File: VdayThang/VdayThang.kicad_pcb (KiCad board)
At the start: 2 copper layers, 101.6 x 101.6 mm, 0 parts

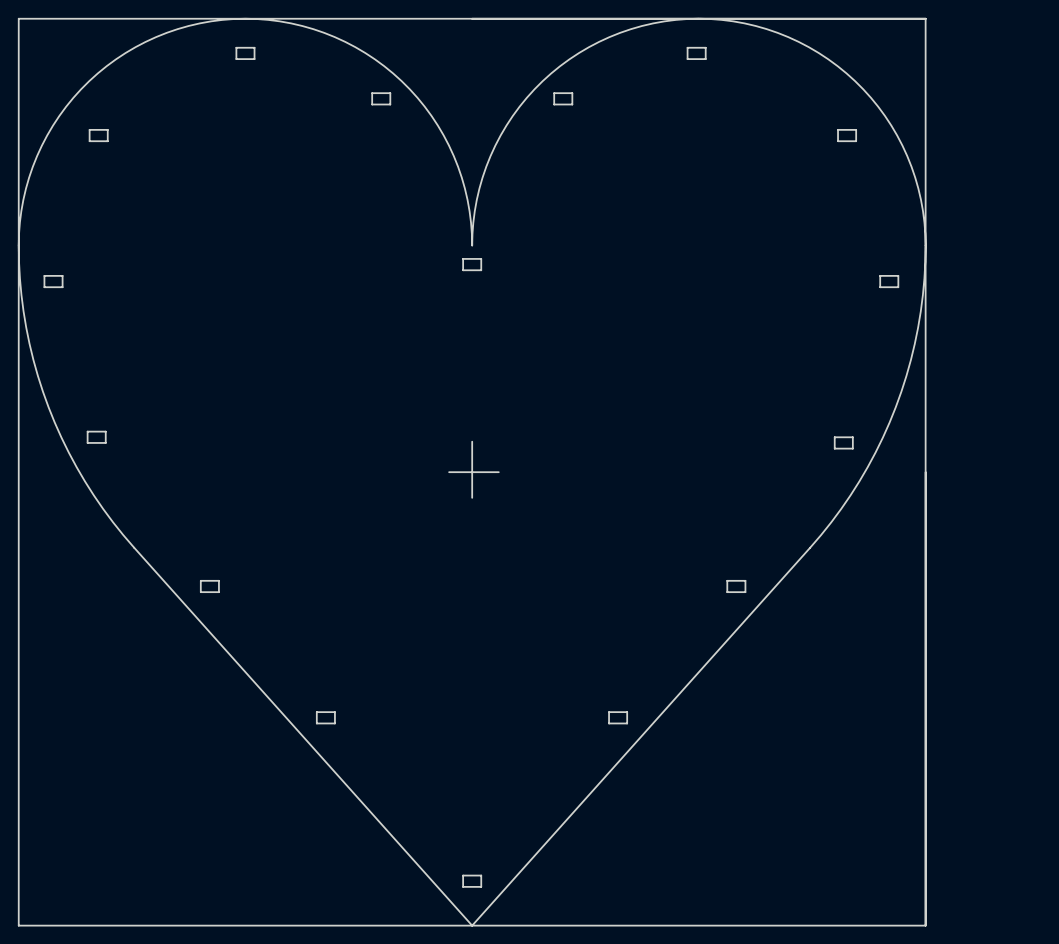
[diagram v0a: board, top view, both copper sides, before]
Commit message: placed footprints
finished basic footprint layout
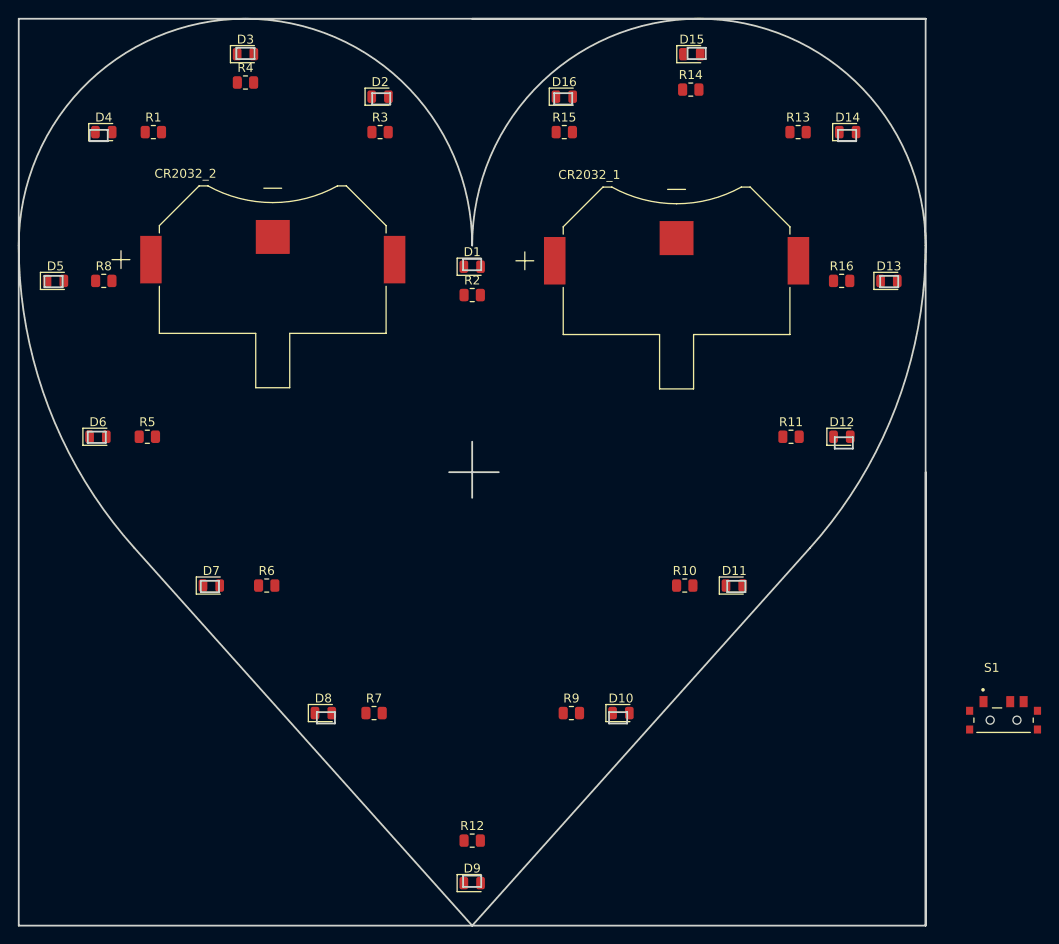
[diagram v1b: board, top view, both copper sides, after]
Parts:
- added CR2032_1: Battery, LogansCustom:BAT_CR2032, F.Cu at (166.6, 70.8)
- added CR2032_2: Battery, LogansCustom:BAT_CR2032, F.Cu at (121.3, 70.6)
- added D1: LED, LED_SMD:LED_0805_2012Metric, F.Cu at (143.7, 71.4)
- added D10: LED, LED_SMD:LED_0805_2012Metric, F.Cu at (160.3, 121.4)
- added D11: LED, LED_SMD:LED_0805_2012Metric, F.Cu at (173.0, 107.2)
- added D12: LED, LED_SMD:LED_0805_2012Metric, F.Cu at (185.1, 90.5)
- added D13: LED, LED_SMD:LED_0805_2012Metric, F.Cu at (190.4, 73.0)
- added D14: LED, LED_SMD:LED_0805_2012Metric, F.Cu at (185.7, 56.4)
- added D15: LED, LED_SMD:LED_0805_2012Metric, F.Cu at (168.3, 47.6)
- added D16: LED, LED_SMD:LED_0805_2012Metric, F.Cu at (154.0, 52.4)
- added D2: LED, LED_SMD:LED_0805_2012Metric, F.Cu at (133.3, 52.4)
- added D3: LED, LED_SMD:LED_0805_2012Metric, F.Cu at (118.3, 47.6)
- added D4: LED, LED_SMD:LED_0805_2012Metric, F.Cu at (102.4, 56.4)
- added D5: LED, LED_SMD:LED_0805_2012Metric, F.Cu at (97.0, 73.0)
- added D6: LED, LED_SMD:LED_0805_2012Metric, F.Cu at (101.7, 90.5)
- added D7: LED, LED_SMD:LED_0805_2012Metric, F.Cu at (114.4, 107.2)
- added D8: LED, LED_SMD:LED_0805_2012Metric, F.Cu at (127.0, 121.4)
- added D9: LED, LED_SMD:LED_0805_2012Metric, F.Cu at (143.7, 140.5)
- added R1: R, Resistor_SMD:R_0805_2012Metric, F.Cu at (108.0, 56.4)
- added R10: R, Resistor_SMD:R_0805_2012Metric, F.Cu at (167.5, 107.2)
- added R11: R, Resistor_SMD:R_0805_2012Metric, F.Cu at (179.4, 90.5)
- added R12: R, Resistor_SMD:R_0805_2012Metric, F.Cu at (143.7, 135.7)
- added R13: R, Resistor_SMD:R_0805_2012Metric, F.Cu at (180.2, 56.4)
- added R14: R, Resistor_SMD:R_0805_2012Metric, F.Cu at (168.2, 51.6)
- added R15: R, Resistor_SMD:R_0805_2012Metric, F.Cu at (154.0, 56.4)
- added R16: R, Resistor_SMD:R_0805_2012Metric, F.Cu at (185.1, 73.0)
- added R2: R, Resistor_SMD:R_0805_2012Metric, F.Cu at (143.7, 74.6)
- added R3: R, Resistor_SMD:R_0805_2012Metric, F.Cu at (133.3, 56.4)
- added R4: R, Resistor_SMD:R_0805_2012Metric, F.Cu at (118.3, 50.8)
- added R5: R, Resistor_SMD:R_0805_2012Metric, F.Cu at (107.3, 90.5)
- added R6: R, Resistor_SMD:R_0805_2012Metric, F.Cu at (120.7, 107.2)
- added R7: R, Resistor_SMD:R_0805_2012Metric, F.Cu at (132.7, 121.4)
- added R8: R, Resistor_SMD:R_0805_2012Metric, F.Cu at (102.4, 73.0)
- added R9: R, Resistor_SMD:R_0805_2012Metric, F.Cu at (154.8, 121.4)
- added S1: SLW-66527511-SMT-TR, LogansCustom:SW_SLW-66527511-SMT-TR, F.Cu at (203.2, 122.2)

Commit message: Routing and Footprints done
Finished routing board, made cr2032 holder footprint. Still need to add edge cuts.
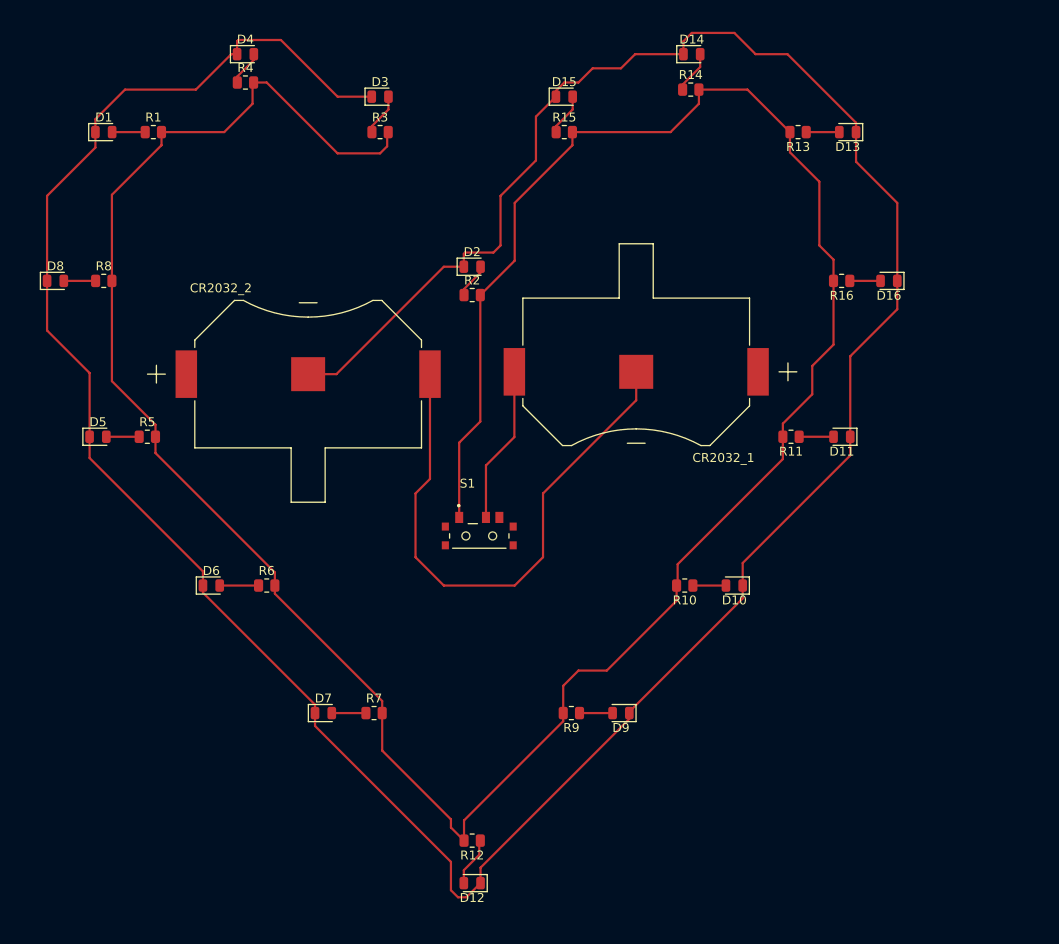
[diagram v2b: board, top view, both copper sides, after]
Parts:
- S1: value SLW-66527511-SMT-TR -> ~
- moved S1 62.3 mm to (144.5, 101.6)
- moved CR2032_2 13.4 mm to (125.3, 83.5)
- moved CR2032_1 13.2 mm to (162.0, 83.2), turned to 180 degrees
- turned D10 to 180 degrees
- turned D11 to 180 degrees
- turned D12 to 180 degrees
- turned D13 to 180 degrees
- turned D16 to 180 degrees
- turned D9 to 180 degrees
- turned R10 to 180 degrees
- turned R11 to 180 degrees
- turned R12 to 180 degrees
- turned R13 to 180 degrees
- turned R16 to 180 degrees
- turned R9 to 180 degrees
- renumbered D4 to D1, D11 to D10, D12 to D11, D9 to D12, D14 to D13, D15 to D14, D16 to D15, D13 to D16, D1 to D2, D2 to D3, D3 to D4, D6 to D5, D7 to D6, D8 to D7, D5 to D8, D10 to D9
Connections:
- S1 pad 1: unconnected-(S1-Pad1) -> 3v
- S1 pad 3: 3v -> unconnected-(S1-Pad3)
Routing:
- net -: track 0.00 -> 345.8 mm
- net 3v: track 0.00 -> 310.2 mm
- net Net-(CR2032_1--): track 0.00 -> 63.2 mm
- net Net-(CR2032_1-+): track 0.00 -> 17.6 mm
- net Net-(D12-A): track 0.00 -> 5.53 mm
- net Net-(D14-A): track 0.00 -> 4.78 mm
- net Net-(D15-A): track 0.00 -> 4.74 mm
- net Net-(D3-A): track 0.00 -> 4.74 mm
- net Net-(D6-A): track 0.00 -> 4.36 mm
- net Net-(D2-A): track 0.00 -> 4.19 mm
- net Net-(D4-A): track 0.00 -> 3.94 mm
- net Net-(D11-A): track 0.00 -> 3.85 mm
- net Net-(D7-A): track 0.00 -> 3.82 mm
- net Net-(D9-A): track 0.00 -> 3.71 mm
- net Net-(D13-A): track 0.00 -> 3.71 mm
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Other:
- board outline removed

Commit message: Finished :0
layout done, BOM done, just need to print, etch, assemble
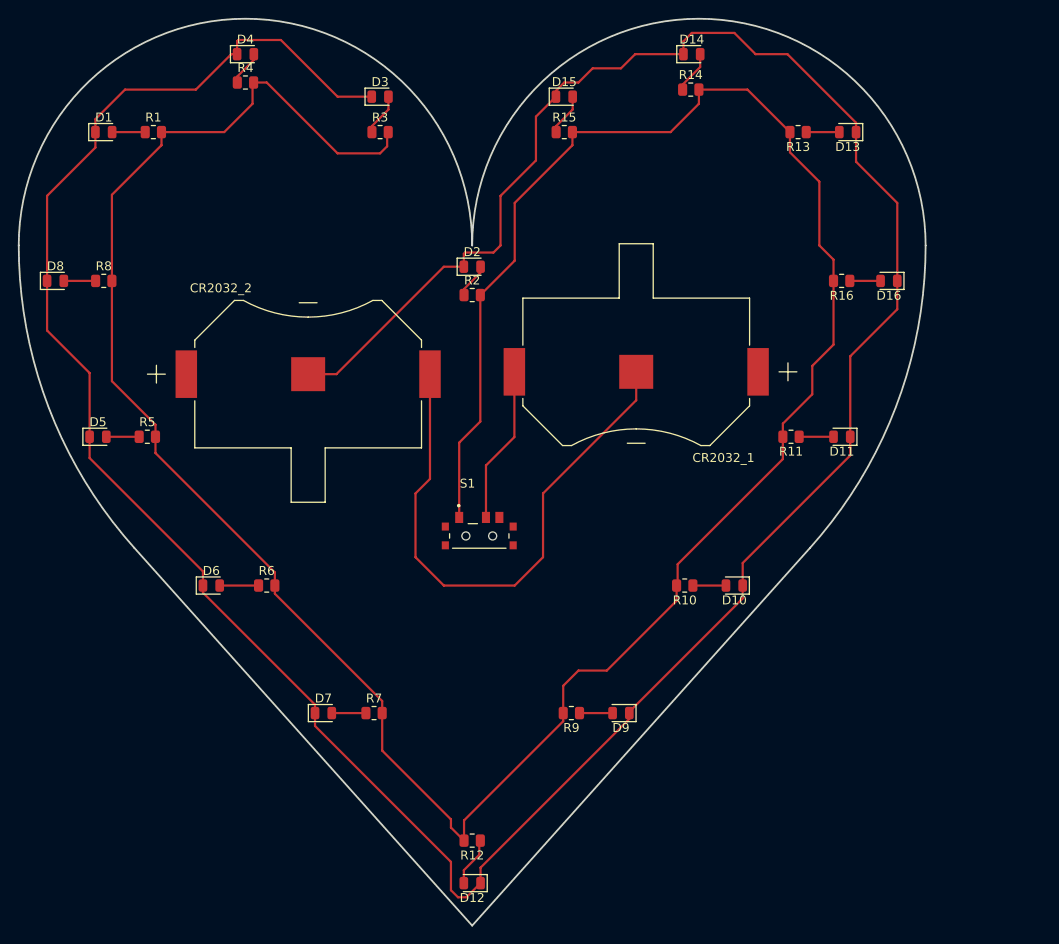
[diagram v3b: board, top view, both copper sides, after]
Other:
- board outline added: 101.6 x 101.6 mm
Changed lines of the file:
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@@
   (gr_line (start 132.464697 51.994282) (end 134.496697 51.994282)
     (stroke (width 0.2) (type solid)) (layer "Dwgs.User"))
+  (gr_line (start 143.66875 145.25625) (end 105.804666 102.922917)
+    (stroke (width 0.2) (type solid)) (layer "Edge.Cuts"))
+  (gr_arc (start 105.804666 102.922917) (mid 96.212794 87.182812) (end 92.86875 69.05625)
+    (stroke (width 0.2) (type solid)) (layer "Edge.Cuts"))
+  (gr_arc (start 194.46875 69.05625) (mid 191.124706 87.182812) (end 181.532834 102.922917)
+    (stroke (width 0.2) (type solid)) (layer "Edge.Cuts"))
+  (gr_line (start 143.66875 145.25625) (end 181.532834 102.922917)
+    (stroke (width 0.2) (type solid)) (layer "Edge.Cuts"))
+  (gr_arc (start 143.66875 69.05625) (mid 169.06875 43.65625) (end 194.46875 69.05625)
+    (stroke (width 0.2) (type solid)) (layer "Edge.Cuts"))
+  (gr_arc (start 92.86875 69.05625) (mid 118.26875 43.65625) (end 143.66875 69.05625)
+    (stroke (width 0.2) (type solid)) (layer "Edge.Cuts"))
   (segment (start 96.04375 63.5) (end 101.45625 58.0875) (width 0.25) (layer "F.Cu") (net 1))
   (segment (start 101.45625 58.0875) (end 101.45625 56.35625) (width 0.25) (layer "F.Cu") (net 1))
@@
     )
   )
+  (group "" (id 627bf66d-ce7d-42bf-90d7-45007c2f4c65)
+    (members
+      10f02e37-6f85-494d-afdb-aa7c09a7e8aa
+      239dcd45-203f-4ea4-99a6-dcb98fbdbb5b
+      24237b50-b826-485d-96d1-f1e5b84721a2
+      276c140d-5e9b-4df4-8011-c8db364865ee
+      4b640248-4e8e-4bb2-9206-12916d5c2009
+      e3077e4a-c645-4bdd-97a3-5d0dfd791ae3
+    )
+  )
